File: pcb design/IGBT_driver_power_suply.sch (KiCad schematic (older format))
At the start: 40 parts, among them Q15 CSD19533Q5A, Q16 CSD19533Q5A, T1 TRANS-3-1CT, U2 LM5030

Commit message: Add footprints, more layout and graphics
Signed-off-by: Marcos Chaparro <mchaparro@paltatech.com>
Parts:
- added C45: 47uF 50v, w_smd_cap:c_elec_6.3x7.7, symbol C-ALUM-6.3mm
- C32, C33, C34, C35: value C-ALUM-6.3mm -> 47uF 50v; footprint pth-passive:C-ALUM-6.3mm -> w_smd_cap:c_elec_6.3x7.7; mfg# (none) -> EEE-FK1H470XP
- D10, D5, D6, D7, D8, D9: value RB160M-60TR -> RB160MM-60TR; footprint (none) -> paltatech:SOD-123F; mfg# RB160M-60TR -> RB160MM-60TR
- DZ2: footprint (none) -> smd-semi:SOD-323F; mfg# (none) -> MM3Z12VB
- R36: value 1k -> 1.15k
- T1: footprint (none) -> paltatech:wurth_750342312; symbol TRANS-3-1CT -> TRANS-wurth_750342312
- TP1, TP2: footprint (none) -> conn-test:TEST-SMD-SMALL
- U2: footprint (none) -> Housings_SSOP:TSSOP-10_3x3mm_Pitch0.5mm
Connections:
- net labels removed: ISOGND_1, ISOGND_2
- wire segments 102 -> 105
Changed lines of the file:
@@
 Sheet 3 4
 Title ""
-Date ""
-Rev ""
-Comp ""
+Date "2016-11-09"
+Rev "A"
+Comp "PALTA TECH"
 Comment1 ""
 Comment2 ""
@@
 Power calculation according to http://www.ti.com/lit/ug/tidu355a/tidu355a.pdf\n0.6W+(0.000000183C*6)*20000Hz*(15v+8v)+(0.000000005500F*6)*20000Hz*(15v+8v)^2 = 1.45 W
 $Comp
-L TRANS-3-1CT T1
-U 1 1 582325EE
+L TRANS-wurth_750342312 T1
+U 3 1 582325EE
 P 6300 3400
 F 0 "T1" H 6377 3446 50  0000 L CNN
 F 1 "TRANS-3-1CT" H 6377 3355 50  0000 L CNN
-F 2 "" H 6300 3450 60  0000 C CNN
+F 2 "paltatech:wurth_750342312" H 6300 3450 60  0001 C CNN
 F 3 "" H 6300 3450 60  0000 C CNN
 F 4 "750342312" H 6300 3400 60  0001 C CNN "mfg#"
-	1    6300 3400
-	1    0    0    -1
-$EndComp
-$Comp
-L TRANS-3-1CT T1
+	3    6300 3400
+	1    0    0    -1
+$EndComp
+$Comp
+L TRANS-wurth_750342312 T1
 U 2 1 5823263E
 P 6000 3650
 F 0 "T1" H 5935 3604 50  0000 R CNN
 F 1 "TRANS-3-1CT" H 5935 3695 50  0000 R CNN
-F 2 "" H 6000 3700 60  0000 C CNN
+F 2 "paltatech:wurth_750342312" H 6000 3700 60  0001 C CNN
 F 3 "" H 6000 3700 60  0000 C CNN
 F 4 "750342312" H 6000 3650 60  0001 C CNN "mfg#"
@@
 $EndComp
 $Comp
-L TRANS-3-1CT T1
-U 3 1 5823267E
+L TRANS-wurth_750342312 T1
+U 1 1 5823267E
 P 6300 5000
 F 0 "T1" H 6377 5046 50  0000 L CNN
 F 1 "TRANS-3-1CT" H 6377 4955 50  0000 L CNN
-F 2 "" H 6300 5050 60  0000 C CNN
+F 2 "paltatech:wurth_750342312" H 6300 5050 60  0001 C CNN
 F 3 "" H 6300 5050 60  0000 C CNN
 F 4 "750342312" H 6300 5000 60  0001 C CNN "mfg#"
-	3    6300 5000
+	1    6300 5000
 	1    0    0    -1
 $EndComp
@@
 F 0 "U2" H 2750 3850 60  0000 C CNN
 F 1 "LM5030" H 2750 4500 60  0000 C CNN
-F 2 "" H 2750 4150 60  0001 C CNN
+F 2 "Housings_SSOP:TSSOP-10_3x3mm_Pitch0.5mm" H 2750 4150 60  0001 C CNN
 F 3 "" H 2750 4150 60  0001 C CNN
 F 4 "LM5030MM/NOPB" H 2850 4250 60  0001 C CNN "mfg#"
@@
 P 7850 3500
 F 0 "D9" H 7770 3454 50  0000 R CNN
-F 1 "RB160M-60TR" H 7770 3545 50  0000 R CNN
-F 2 "" H 7850 3500 60  0000 C CNN
+F 1 "RB160MM-60TR" H 7770 3545 50  0000 R CNN
+F 2 "paltatech:SOD-123F" H 7850 3500 60  0001 C CNN
 F 3 "" H 7850 3500 60  0000 C CNN
-F 4 "RB160M-60TR" H 7850 3500 60  0001 C CNN "mfg#"
+F 4 "RB160MM-60TR" H 7850 3500 60  0001 C CNN "mfg#"
 	1    7850 3500
 	0    1    1    0
@@
 P 7300 2800
 F 0 "D6" H 7220 2754 50  0000 R CNN
-F 1 "RB160M-60TR" H 7220 2845 50  0000 R CNN
-F 2 "" H 7300 2800 60  0000 C CNN
+F 1 "RB160MM-60TR" H 7220 2845 50  0000 R CNN
+F 2 "paltatech:SOD-123F" H 7300 2800 60  0001 C CNN
 F 3 "" H 7300 2800 60  0000 C CNN
-F 4 "RB160M-60TR" H 7300 2800 60  0001 C CNN "mfg#"
+F 4 "RB160MM-60TR" H 7300 2800 60  0001 C CNN "mfg#"
 	1    7300 2800
 	-1   0    0    1
@@
 P 7300 2500
 F 0 "D5" H 7220 2454 50  0000 R CNN
-F 1 "RB160M-60TR" H 7220 2545 50  0000 R CNN
-F 2 "" H 7300 2500 60  0000 C CNN
+F 1 "RB160MM-60TR" H 7220 2545 50  0000 R CNN
+F 2 "paltatech:SOD-123F" H 7300 2500 60  0001 C CNN
 F 3 "" H 7300 2500 60  0000 C CNN
-F 4 "RB160M-60TR" H 7300 2500 60  0001 C CNN "mfg#"
+F 4 "RB160MM-60TR" H 7300 2500 60  0001 C CNN "mfg#"
 	1    7300 2500
 	-1   0    0    1
@@
 F 0 "DZ2" H 2750 3450 50  0000 L CNN
 F 1 "12v zener" H 2500 3350 50  0000 L CNN
-F 2 "" H 2950 3400 60  0000 C CNN
+F 2 "smd-semi:SOD-323F" H 2950 3400 60  0001 C CNN
 F 3 "" H 2950 3400 60  0000 C CNN
+F 4 "MM3Z12VB" H 2950 3400 60  0001 C CNN "mfg#"
 	1    2950 3400
 	1    0    0    -1
@@
 P 2950 3050
 F 0 "R36" H 3013 3096 50  0000 L CNN
-F 1 "1k" H 3013 3005 50  0000 L CNN
+F 1 "1.15k" H 3013 3005 50  0000 L CNN
 F 2 "IPC7351-Nominal:RESC1608X50" H 2950 3050 50  0001 C CNN
 F 3 "" H 2950 3100 60  0000 C CNN
@@
 Text GLabel 2700 2750 0    50   Input ~ 0
 24v
-Text GLabel 5950 3650 0    50   Input ~ 0
+Text GLabel 5550 2800 0    50   Input ~ 0
 24v
 Text Label 3900 4750 2    60   ~ 0
@@
 F 0 "TP1" H 5410 3621 50  0000 L CNN
 F 1 "TESTPOINT" H 5410 3530 50  0000 L CNN
-F 2 "" H 5350 3500 50  0000 C CNN
+F 2 "conn-test:TEST-SMD-SMALL" H 5350 3500 50  0001 C CNN
 F 3 "" H 5350 3500 50  0000 C CNN
 	1    5350 3500
@@
 F 0 "TP2" H 5510 3621 50  0000 L CNN
 F 1 "TESTPOINT" H 5510 3530 50  0000 L CNN
-F 2 "" H 5450 3500 50  0000 C CNN
+F 2 "conn-test:TEST-SMD-SMALL" H 5450 3500 50  0001 C CNN
 F 3 "" H 5450 3500 50  0000 C CNN
 	1    5450 3500
@@
 Wire Wire Line
 	6300 3050 10400 3050
-$Comp
-L ISOGND_1 #PWR013
-U 1 1 5823AA14
-P 10050 3100
-F 0 "#PWR013" H 10050 3100 30  0001 C CNN
-F 1 "ISOGND_1" H 10050 3100 30  0001 C CNN
-F 2 "" H 10050 3100 60  0000 C CNN
-F 3 "" H 10050 3100 60  0000 C CNN
-	1    10050 3100
-	1    0    0    -1
-$EndComp
-$Comp
-L ISOGND_2 #PWR014
-U 1 1 5823ACF6
-P 10050 4850
-F 0 "#PWR014" H 10050 4850 30  0001 C CNN
-F 1 "ISOGND_2" H 10050 4850 30  0001 C CNN
-F 2 "" H 10050 4850 60  0000 C CNN
-F 3 "" H 10050 4850 60  0000 C CNN
-	1    10050 4850
-	1    0    0    -1
-$EndComp
 Wire Wire Line
 	6300 3500 7750 3500
@@
 P 9500 3300
 F 0 "C33" H 9613 3346 50  0000 L CNN
-F 1 "C-ALUM-6.3mm" H 9613 3255 50  0000 L CNN
-F 2 "pth-passive:C-ALUM-6.3mm" H 9500 3300 50  0001 C CNN
+F 1 "47uF 50v" H 9613 3255 50  0000 L CNN
+F 2 "w_smd_cap:c_elec_6.3x7.7" H 9500 3300 50  0001 C CNN
 F 3 "" H 9490 3275 60  0000 C CNN
+F 4 "EEE-FK1H470XP" H 9500 3300 60  0001 C CNN "mfg#"
 	1    9500 3300
 	1    0    0    -1
@@
 P 9500 2800
 F 0 "C32" H 9613 2846 50  0000 L CNN
-F 1 "C-ALUM-6.3mm" H 9613 2755 50  0000 L CNN
-F 2 "pth-passive:C-ALUM-6.3mm" H 9500 2800 50  0001 C CNN
+F 1 "47uF 50v" H 9613 2755 50  0000 L CNN
+F 2 "w_smd_cap:c_elec_6.3x7.7" H 9500 2800 50  0001 C CNN
 F 3 "" H 9490 2775 60  0000 C CNN
+F 4 "EEE-FK1H470XP" H 9500 2800 60  0001 C CNN "mfg#"
 	1    9500 2800
 	1    0    0    -1
@@
 Text HLabel 10400 3050 2    60   Input ~ 0
 GND_TOP
-Wire Wire Line
-	10050 3100 10050 3050
-Connection ~ 10050 3050
 Text HLabel 10400 3500 2    60   Input ~ 0
 -8V_TOP
@@
 P 7850 5250
 F 0 "D10" H 7770 5204 50  0000 R CNN
-F 1 "RB160M-60TR" H 7770 5295 50  0000 R CNN
-F 2 "" H 7850 5250 60  0000 C CNN
+F 1 "RB160MM-60TR" H 7770 5295 50  0000 R CNN
+F 2 "paltatech:SOD-123F" H 7850 5250 60  0001 C CNN
 F 3 "" H 7850 5250 60  0000 C CNN
-F 4 "RB160M-60TR" H 7850 5250 60  0001 C CNN "mfg#"
+F 4 "RB160MM-60TR" H 7850 5250 60  0001 C CNN "mfg#"
 	1    7850 5250
 	0    1    1    0
@@
 P 7300 4550
 F 0 "D8" H 7220 4504 50  0000 R CNN
-F 1 "RB160M-60TR" H 7220 4595 50  0000 R CNN
-F 2 "" H 7300 4550 60  0000 C CNN
+F 1 "RB160MM-60TR" H 7220 4595 50  0000 R CNN
+F 2 "paltatech:SOD-123F" H 7300 4550 60  0001 C CNN
 F 3 "" H 7300 4550 60  0000 C CNN
-F 4 "RB160M-60TR" H 7300 4550 60  0001 C CNN "mfg#"
+F 4 "RB160MM-60TR" H 7300 4550 60  0001 C CNN "mfg#"
 	1    7300 4550
 	-1   0    0    1
@@
 P 7300 4250
 F 0 "D7" H 7220 4204 50  0000 R CNN
-F 1 "RB160M-60TR" H 7220 4295 50  0000 R CNN
-F 2 "" H 7300 4250 60  0000 C CNN
+F 1 "RB160MM-60TR" H 7220 4295 50  0000 R CNN
+F 2 "paltatech:SOD-123F" H 7300 4250 60  0001 C CNN
 F 3 "" H 7300 4250 60  0000 C CNN
-F 4 "RB160M-60TR" H 7300 4250 60  0001 C CNN "mfg#"
+F 4 "RB160MM-60TR" H 7300 4250 60  0001 C CNN "mfg#"
 	1    7300 4250
 	-1   0    0    1
@@
 P 9500 5050
 F 0 "C35" H 9613 5096 50  0000 L CNN
-F 1 "C-ALUM-6.3mm" H 9613 5005 50  0000 L CNN
-F 2 "pth-passive:C-ALUM-6.3mm" H 9500 5050 50  0001 C CNN
+F 1 "47uF 50v" H 9613 5005 50  0000 L CNN
+F 2 "w_smd_cap:c_elec_6.3x7.7" H 9500 5050 50  0001 C CNN
 F 3 "" H 9490 5025 60  0000 C CNN
+F 4 "EEE-FK1H470XP" H 9500 5050 60  0001 C CNN "mfg#"
 	1    9500 5050
 	1    0    0    -1
@@
 P 9500 4550
 F 0 "C34" H 9613 4596 50  0000 L CNN
-F 1 "C-ALUM-6.3mm" H 9613 4505 50  0000 L CNN
-F 2 "pth-passive:C-ALUM-6.3mm" H 9500 4550 50  0001 C CNN
+F 1 "47uF 50v" H 9613 4505 50  0000 L CNN
+F 2 "w_smd_cap:c_elec_6.3x7.7" H 9500 4550 50  0001 C CNN
 F 3 "" H 9490 4525 60  0000 C CNN
+F 4 "EEE-FK1H470XP" H 9500 4550 60  0001 C CNN "mfg#"
 	1    9500 4550
 	1    0    0    -1
@@
 Text HLabel 10400 4800 2    60   Input ~ 0
 GND_BOTTOM
-Wire Wire Line
-	10050 4850 10050 4800
-Connection ~ 10050 4800
 Text HLabel 10400 5250 2    60   Input ~ 0
 -8V_BOTTOM
@@
 Wire Wire Line
 	6300 5100 6300 5250
+Wire Wire Line
+	5900 3650 5950 3650
+Wire Wire Line
+	5900 2800 5900 3650
+$Comp
+L C-ALUM-6.3mm C45
+U 1 1 58273A86
+P 5650 3000
+F 0 "C45" H 5763 3046 50  0000 L CNN
+F 1 "47uF 50v" H 5763 2955 50  0000 L CNN
+F 2 "w_smd_cap:c_elec_6.3x7.7" H 5650 3000 50  0001 C CNN
+F 3 "" H 5640 2975 60  0000 C CNN
+F 4 "EEE-FK1H470XP" H 5650 3000 60  0001 C CNN "mfg#"
+	1    5650 3000
+	-1   0    0    -1
+$EndComp
+Wire Wire Line
+	5550 2800 5900 2800
+Wire Wire Line
+	5650 2800 5650 2900
+Connection ~ 5650 2800
+$Comp
+L GND #PWR013
+U 1 1 5827420A
+P 5650 3150
+F 0 "#PWR013" H 5650 3150 30  0001 C CNN
+F 1 "GND" H 5650 3080 30  0001 C CNN
+F 2 "" H 5650 3150 60  0000 C CNN
+F 3 "" H 5650 3150 60  0000 C CNN
+	1    5650 3150
+	1    0    0    -1
+$EndComp
+Wire Wire Line
+	5650 3150 5650 3100
 $EndSCHEMATC

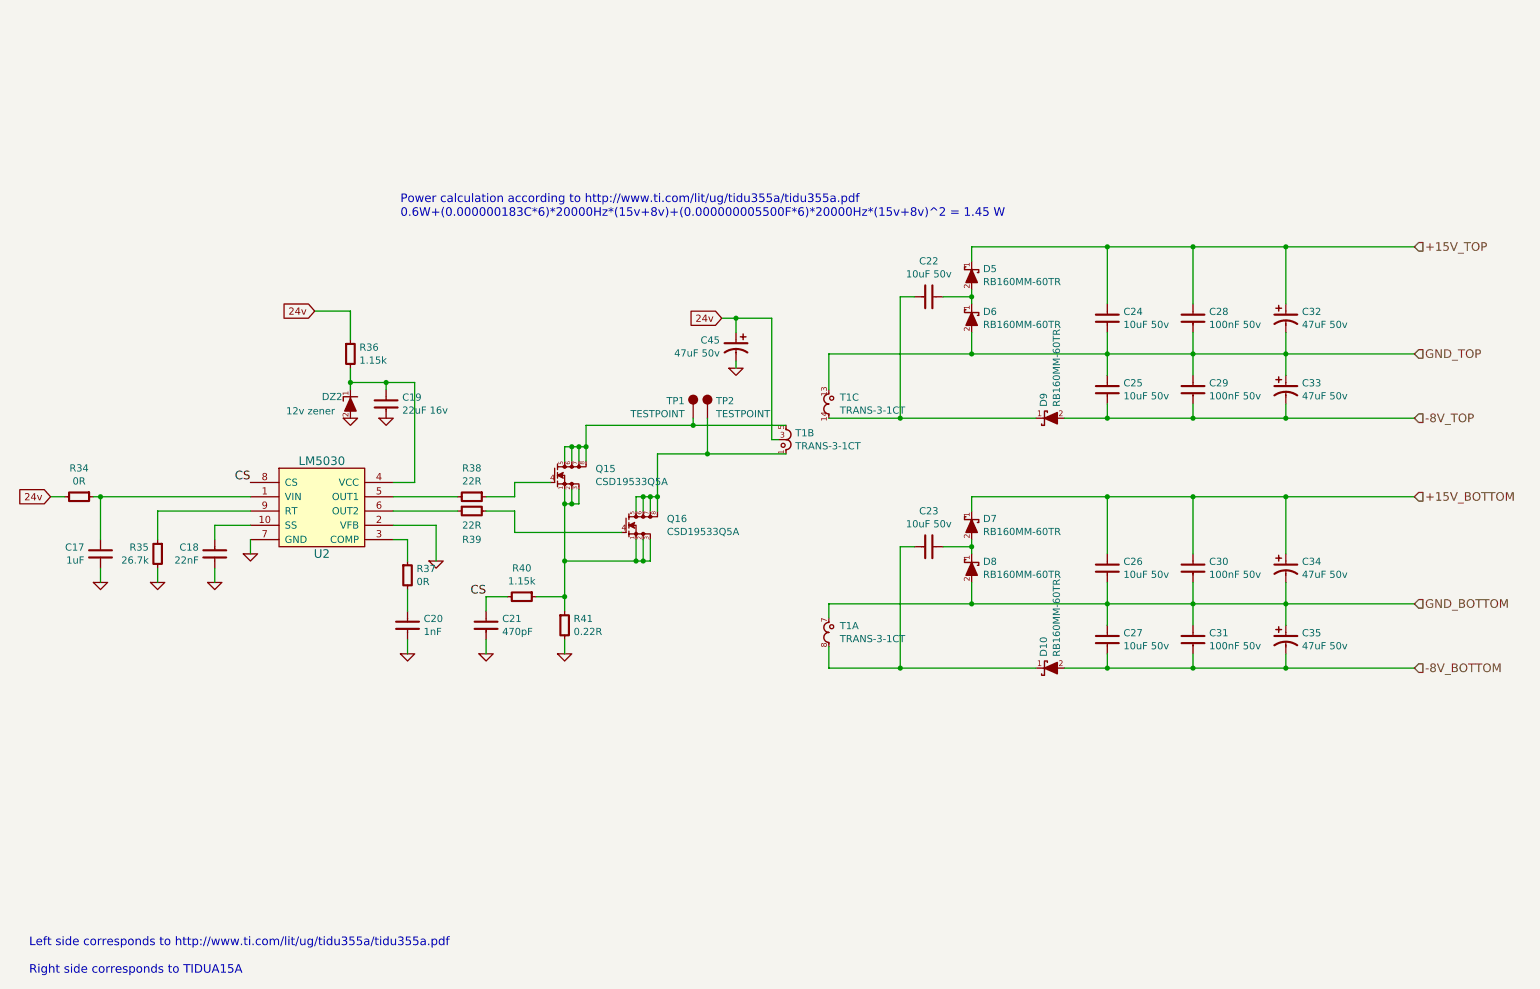
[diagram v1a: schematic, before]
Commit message: Larger gate resistors, added gate caps, added comments and images to the schematic
Signed-off-by: Marcos Chaparro <mchaparro@paltatech.com>
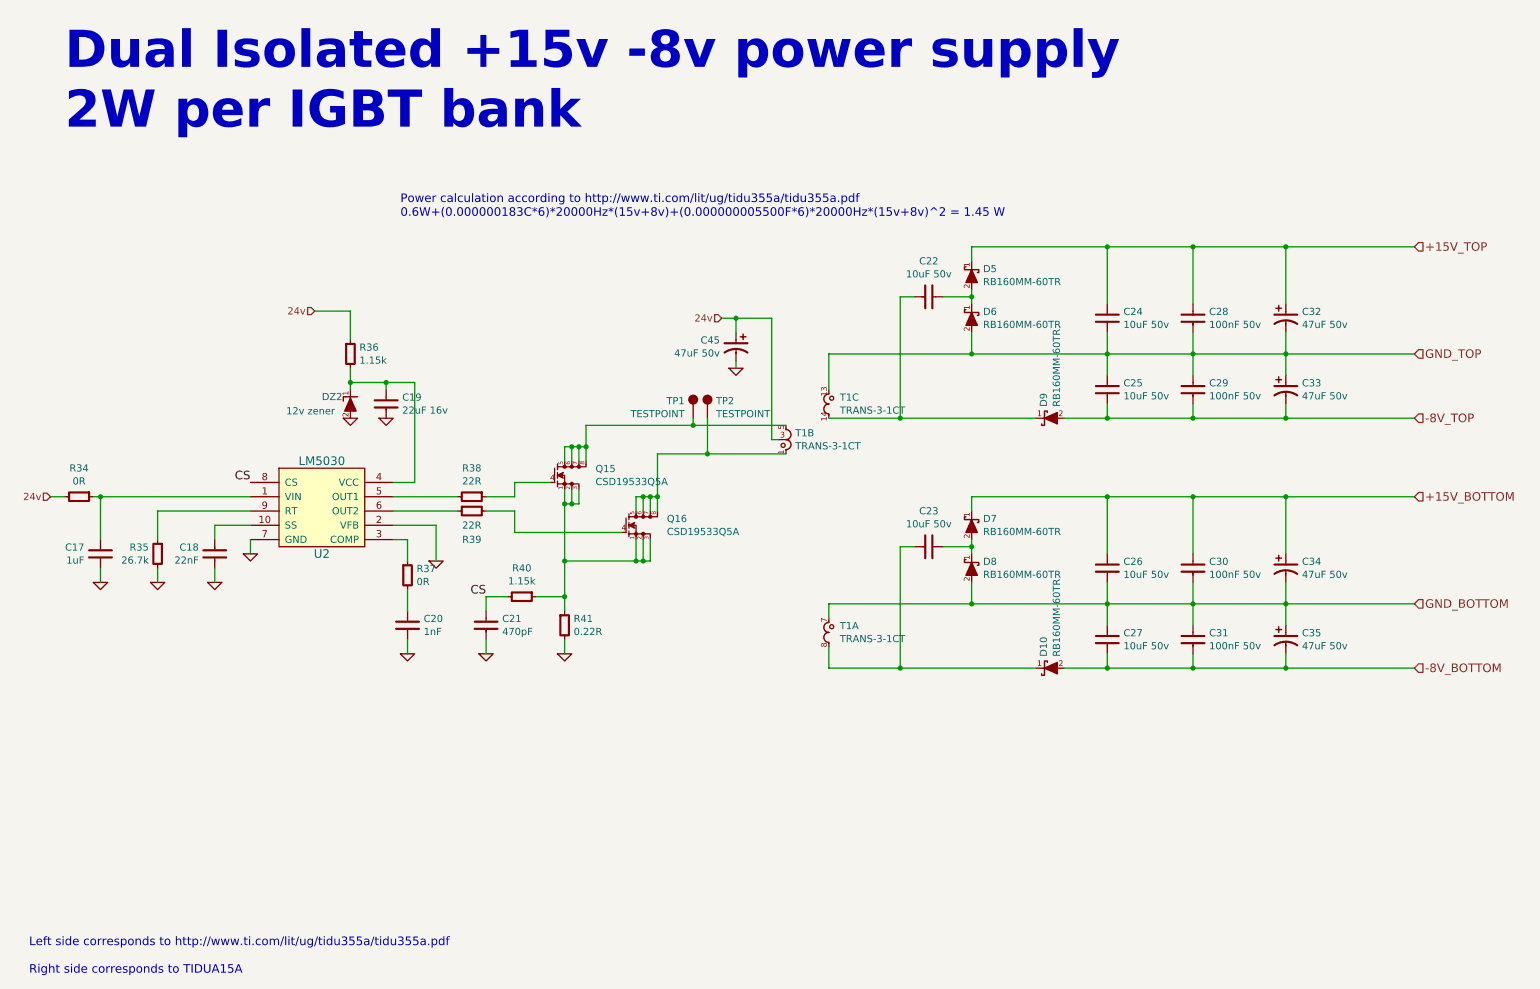
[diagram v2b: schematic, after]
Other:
- note added: "Dual Isolated +15v -8v power supply\n2W per IGBT bank"
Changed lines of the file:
@@
 LIBS:paltatech
 LIBS:IGBT_board-cache
-EELAYER 25 0
+EELAYER 26 0
 EELAYER END
 $Descr A4 11693 8268
@@
 Date "2016-11-09"
 Rev "A"
-Comp "PALTA TECH"
+Comp "PALTA TECH S.A."
 Comment1 ""
 Comment2 ""
@@
 	1    0    0    -1
 $EndComp
-Text GLabel 2700 2750 0    50   Input ~ 0
-24v
-Text GLabel 5550 2800 0    50   Input ~ 0
-24v
 Text Label 3900 4750 2    60   ~ 0
 CS
@@
 	1    0    0    1
 $EndComp
-Text GLabel 850  4050 0    50   Input ~ 0
-24v
 $Comp
 L GND #PWR010
@@
 Wire Wire Line
 	5650 3150 5650 3100
+Text Notes 950  1500 0    260  ~ 52
+Dual Isolated +15v -8v power supply\n2W per IGBT bank
+Text HLabel 5550 2800 0    50   Input ~ 0
+24v
+Text HLabel 2700 2750 0    50   Input ~ 0
+24v
+Text HLabel 850  4050 0    50   Input ~ 0
+24v
 $EndSCHEMATC
